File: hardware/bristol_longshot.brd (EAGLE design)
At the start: 12 x 50 mm, 42 parts, among them U1 SAM_D20E, U2 SI4060, U4 ADP1607ACPZN-R7, U5 S25FS-S

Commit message: Merge
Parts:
- added JP1: (no value), SparkFun:1X04_LOCK
- added JP2: (no value), SparkFun:1X06_LOCK
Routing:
- net !MR: track 21.5 -> 26.5 mm
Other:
- board size 12 x 50 mm -> 16 x 50 mm
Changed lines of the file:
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@@
 <setting verticaltext="up"/>
 </settings>
-<grid distance="0.125" unitdist="mm" unit="mm" style="lines" multiple="1" display="yes" altdistance="0.025" altunitdist="inch" altunit="inch"/>
+<grid distance="1" unitdist="mm" unit="mm" style="lines" multiple="1" display="yes" altdistance="0.025" altunitdist="inch" altunit="inch"/>
 <layers>
 <layer number="1" name="Top" color="4" fill="1" visible="yes" active="yes"/>
@@
 </polygon>
 <wire x1="0" y1="0" x2="0" y2="50" width="0" layer="20"/>
-<wire x1="0" y1="50" x2="12" y2="50" width="0" layer="20"/>
-<wire x1="12" y1="50" x2="12" y2="0" width="0" layer="20"/>
-<wire x1="12" y1="0" x2="0" y2="0" width="0" layer="20"/>
+<wire x1="0" y1="50" x2="16" y2="50" width="0" layer="20"/>
+<wire x1="16" y1="50" x2="16" y2="0" width="0" layer="20"/>
+<wire x1="16" y1="0" x2="0" y2="0" width="0" layer="20"/>
 <text x="10.25" y="31.5" size="0.762" layer="113" font="vector" ratio="20" rot="MR90">XxXxXxXxXxXx</text>
 <text x="10" y="24.375" size="0.635" layer="21" font="vector" ratio="16" rot="R270">100nF100pF</text>
@@
 <element name="ESD1" library="microbuilder_v3" package="_0603MP" value="0.25pF" x="10" y="45.25" rot="R180"/>
 <element name="ESD2" library="microbuilder_v3" package="_0603MP" value="0.25pF" x="7.75" y="4.125" rot="R180"/>
+<element name="JP1" library="SparkFun" package="1X04_LOCK" value="" x="14" y="31" rot="R90"/>
+<element name="JP2" library="SparkFun" package="1X06_LOCK" value="" x="14" y="12" rot="R90"/>
 </elements>
 <signals>
@@
 <wire x1="11" y1="23.375" x2="11" y2="27.125" width="0.1524" layer="16"/>
 <wire x1="11" y1="27.125" x2="10.125" y2="28" width="0.1524" layer="16"/>
+<wire x1="11" y1="23.375" x2="10.875" y2="27.25" width="0.1524" layer="16"/>
+<wire x1="10.875" y1="27.25" x2="10.125" y2="28" width="0.1524" layer="16"/>
 <wire x1="10.125" y1="28" x2="6.25" y2="28" width="0.1524" layer="16"/>
 </signal>

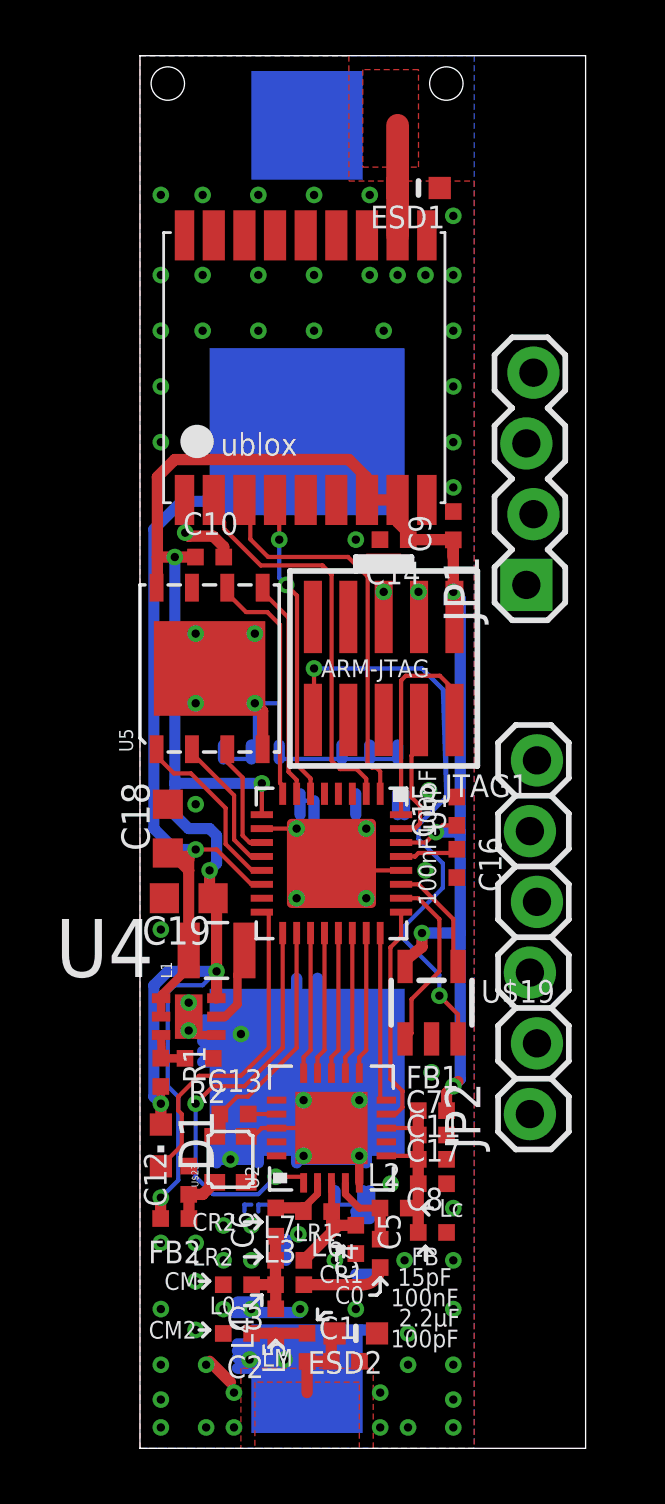
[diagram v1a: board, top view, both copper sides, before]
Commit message: Rocketry board layout complete, todo: Adjust buck reference for higher vcc
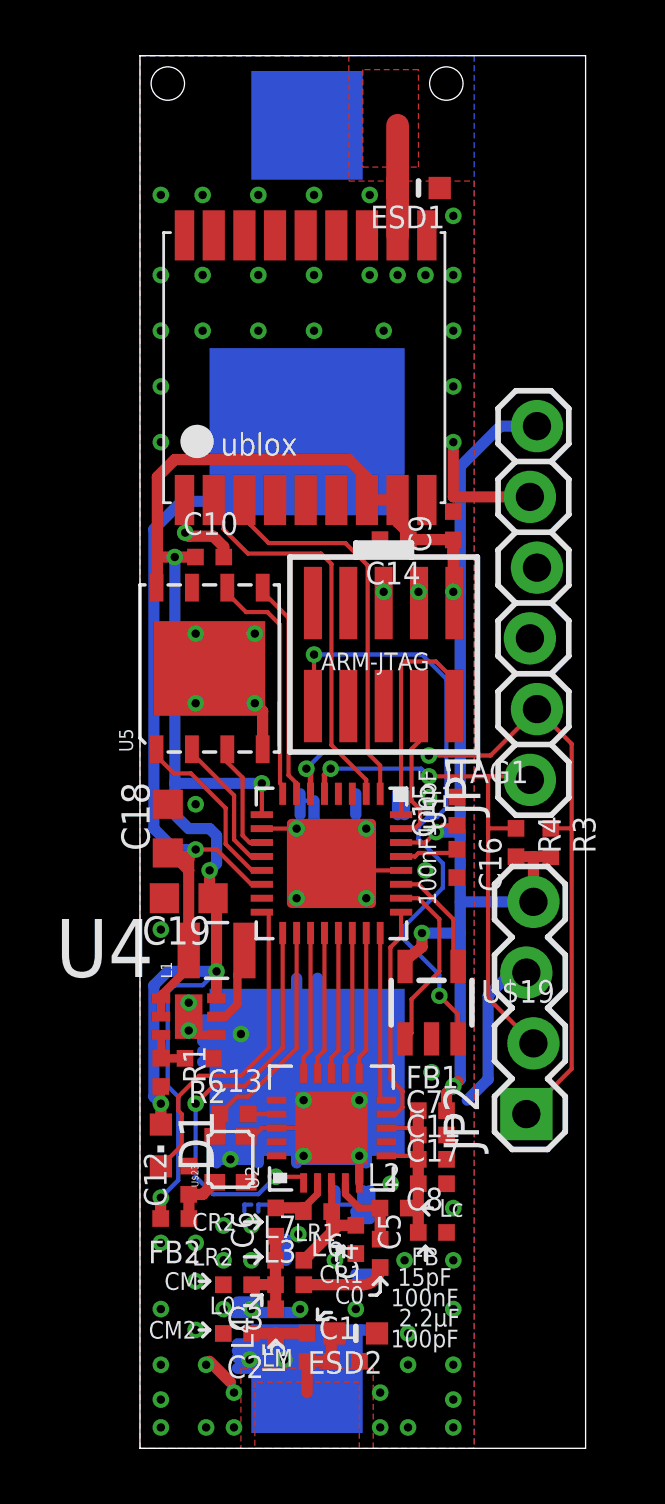
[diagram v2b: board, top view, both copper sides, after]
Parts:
- added R3, R4: 10kΩ, microbuilder_v3:_0402
- JP1: device SparkFun:1X04_LOCK -> SparkFun:1X06_LOCK
- JP2: device SparkFun:1X06_LOCK -> SparkFun:1X04_LOCK
- moved JP1 7.00 mm to (14.0, 24.0)
- moved JTAG1 0.50 mm to (8.75, 28.5)
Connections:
- removed net TIMEPULSE: U$48.4_TIMEPULSE, U1.6
- new net SCL: JP1.2, JP2.1, R3.1, U1.6
- new net SDA: JP1.1, JP2.2, R4.1, U1.5
- net 1.8V: now also JP1.6, JP2.4, R3.2, R4.2
- net GND: now also JP1.5, JP2.3
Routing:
- net SCL: track 0.00 -> 26.7 mm, vias 0 -> 2
- net SDA: track 0.00 -> 19.6 mm, vias 0 -> 2
- net 1.8V: track 87.6 -> 101.5 mm
- net TIMEPULSE: track 11.0 -> 0.00 mm, vias 2 -> 0
- net !MR: track 26.5 -> 23.1 mm
- net GND: track 74.6 -> 74.4 mm, vias 87 -> 85
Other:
- board text removed: "XxXxXxXxXxXx"
